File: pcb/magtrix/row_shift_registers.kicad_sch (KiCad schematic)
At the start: 2 parts, among them U2 74HC595, U5 74HC595

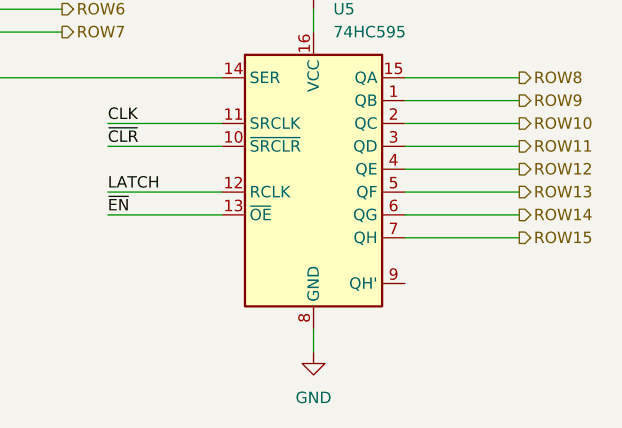
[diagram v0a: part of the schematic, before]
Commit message: Finished schematics and footprints, need to redo the placement
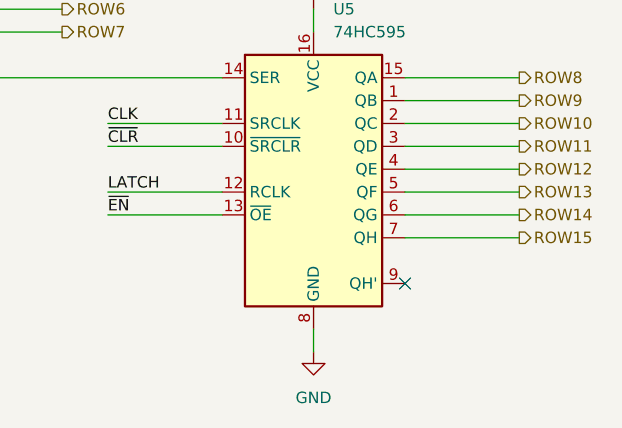
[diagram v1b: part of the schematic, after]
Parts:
- U2, U5: footprint (none) -> SHIFT_REGISTER:SOIC127P600X175-16N; MFR (none) -> 74HC595D(BJ); MOUSER (none) -> 757-74HC595DBJ
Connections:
- no-connect marks 0 -> 1
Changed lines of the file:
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@@
 	(generator_version "8.0")
 	(paper "A5")
+	(no_connect
+		(at 148.59 81.28)
+	)
 	(wire
 		(pts
@@
 			)
 		)
-		(property "Footprint" ""
+		(property "Footprint" "SHIFT_REGISTER:SOIC127P600X175-16N"
 			(at 138.43 68.58 0)
 			(effects
@@
 		)
 		(property "Description" "8-bit serial in/out Shift Register 3-State Outputs"
+			(at 138.43 68.58 0)
+			(effects
+				(font
+					(size 1.27 1.27)
+				)
+				(hide yes)
+			)
+		)
+		(property "MFR" "74HC595D(BJ) "
+			(at 138.43 68.58 0)
+			(effects
+				(font
+					(size 1.27 1.27)
+				)
+				(hide yes)
+			)
+		)
+		(property "MOUSER" "757-74HC595DBJ "
 			(at 138.43 68.58 0)
 			(effects
@@
 			)
 		)
-		(property "Footprint" ""
+		(property "Footprint" "SHIFT_REGISTER:SOIC127P600X175-16N"
 			(at 87.63 45.72 0)
 			(effects
@@
 			(at 87.63 45.72 0)
 			(effects
+				(font
+					(size 1.27 1.27)
+				)
+				(hide yes)
+			)
+		)
+		(property "MFR" "74HC595D(BJ) "
+			(at 87.63 45.72 0)
+			(effects
+				(font
+					(size 1.27 1.27)
+				)
+				(hide yes)
+			)
+		)
+		(property "MOUSER" "757-74HC595DBJ "
+			(at 87.63 45.72 0)
+			(effects

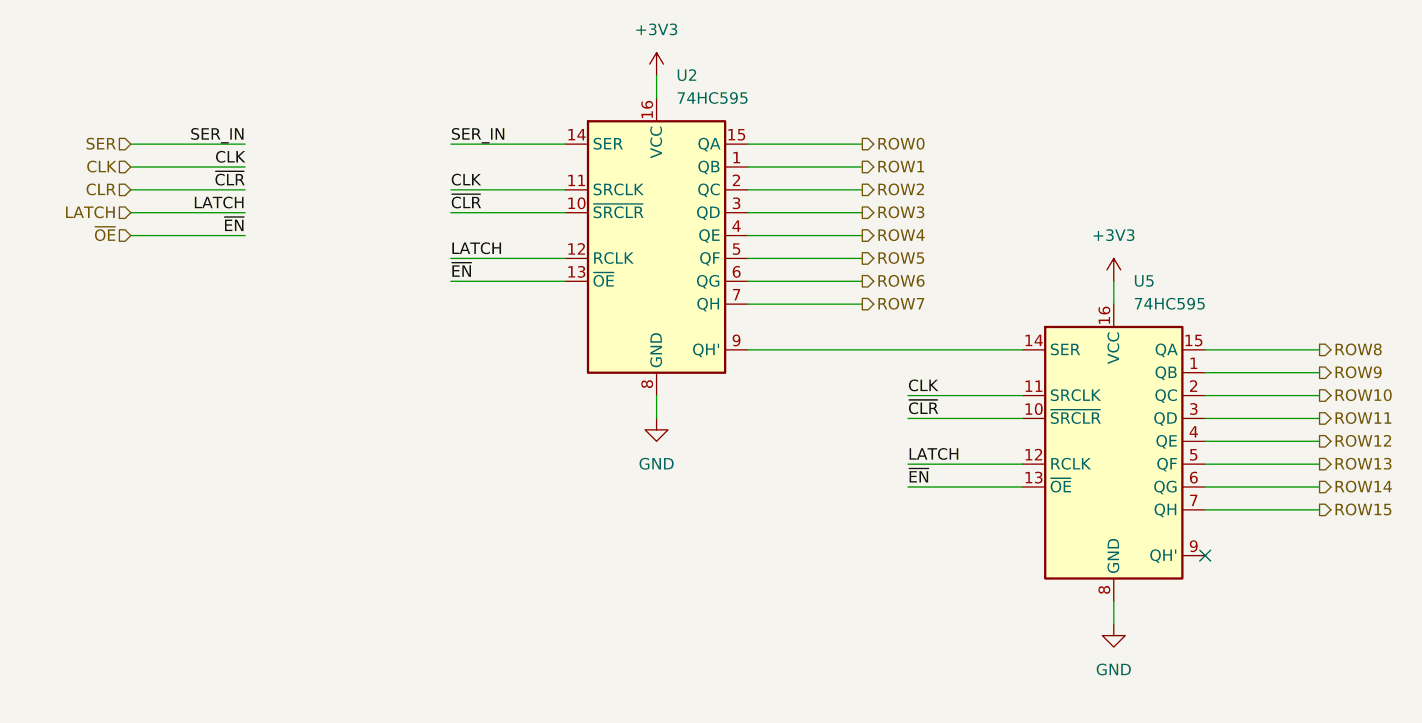
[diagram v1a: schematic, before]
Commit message: Changed shift registers to open drain ones
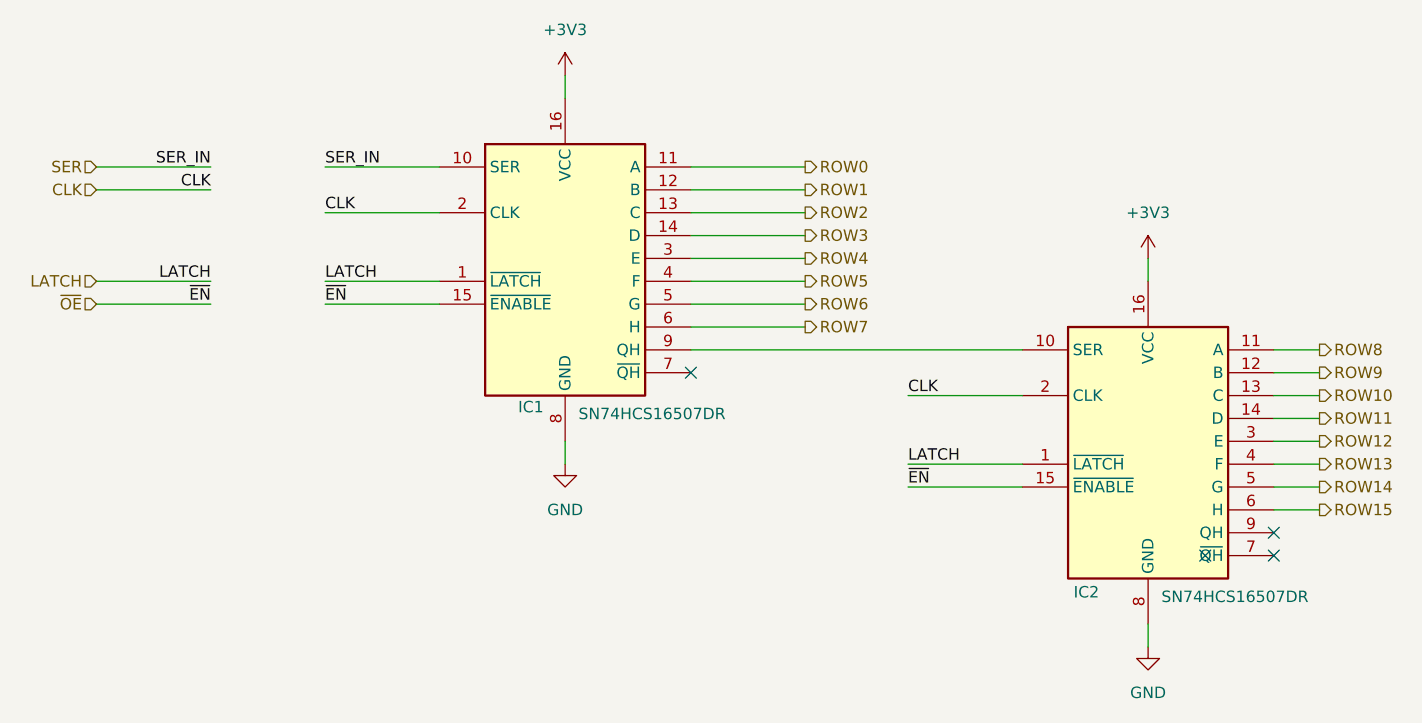
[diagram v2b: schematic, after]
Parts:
- removed U2, U5: 74HC595, SHIFT_REGISTER:SOIC127P600X175-16N, symbol 74xx:74HC595
- added IC1, IC2: SN74HCS16507DR, SOIC127P600X175-16N, symbol SN74HCS16507DR:SN74HCS16507DR
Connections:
- net +3V3: now also IC1.16 (VCC), IC2.16 (VCC)
- net CLK: now also IC1.2 (CLK), IC2.2 (CLK)
- net GND: now also IC1.8 (GND), IC2.8 (GND)
- net LATCH: now also IC1.1 (~{LATCH}), IC2.1 (~{LATCH})
- net ROW0: now also IC1.11 (A)
- net ROW1: now also IC1.12 (B)
- net ROW10: now also IC2.13 (C)
- net ROW11: now also IC2.14 (D)
- net ROW12: now also IC2.3 (E)
- net ROW13: now also IC2.4 (F)
- net ROW14: now also IC2.5 (G)
- net ROW15: now also IC2.6 (H)
- net ROW2: now also IC1.13 (C)
- net ROW3: now also IC1.14 (D)
- net ROW4: now also IC1.3 (E)
- net ROW5: now also IC1.4 (F)
- net ROW6: now also IC1.5 (G)
- net ROW7: now also IC1.6 (H)
- net ROW8: now also IC2.11 (A)
- net ROW9: now also IC2.12 (B)
- net SER: now also IC1.10 (SER)
- net ~{OE}: now also IC1.15 (~{ENABLE}), IC2.15 (~{ENABLE})
- new net: IC1.9 (QH), IC2.10 (SER)
- no-connect marks 1 -> 4

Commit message: Added finished PCB
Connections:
- net ROW13: no longer names the net of IC2.4 (F)
- net ROW14: no longer names the net of IC2.5 (G)
- net ROW15: no longer names the net of IC2.6 (H)
- no-connect marks 4 -> 7
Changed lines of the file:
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@@
+	)
+	(no_connect
+		(at 156.21 73.66)
 	)
 	(no_connect
@@
 		(at 156.21 81.28)
 	)
-	(wire
-		(pts
-			(xy 156.21 73.66) (xy 161.29 73.66)
-		)
-		(stroke
-			(width 0)
-			(type default)
-		)
+	(no_connect
+		(at 156.21 76.2)
+	)
+	(no_connect
+		(at 156.21 71.12)
 	)
 	(wire
@@
 	(wire
 		(pts
-			(xy 156.21 76.2) (xy 161.29 76.2)
-		)
-		(stroke
-			(width 0)
-			(type default)
-		)
-	)
-	(wire
-		(pts
 			(xy 91.44 48.26) (xy 104.14 48.26)
 		)
@@
 		(pts
 			(xy 91.44 43.18) (xy 104.14 43.18)
-		)
-		(stroke
-			(width 0)
-			(type default)
-		)
-	)
-	(wire
-		(pts
-			(xy 156.21 71.12) (xy 161.29 71.12)
 		)
 		(stroke
@@
 		(shape output)
 		(at 104.14 48.26 0)
-		(fields_autoplaced yes)
-		(effects
-			(font
-				(size 1.27 1.27)
-			)
-			(justify left)
-		)
-	)
-	(hierarchical_label "ROW13"
-		(shape output)
-		(at 161.29 71.12 0)
 		(fields_autoplaced yes)
 		(effects
@@
 		)
 	)
-	(hierarchical_label "ROW14"
-		(shape output)
-		(at 161.29 73.66 0)
-		(fields_autoplaced yes)
-		(effects
-			(font
-				(size 1.27 1.27)
-			)
-			(justify left)
-		)
-	)
 	(hierarchical_label "SER"
 		(shape input)
@@
 		(fields_autoplaced yes)
 		(effects
-			(font
-				(size 1.27 1.27)
-			)
-			(justify left)
-		)
-	)
-	(hierarchical_label "ROW15"
-		(shape output)
-		(at 161.29 76.2 0)
-		(fields_autoplaced yes)
-		(effects
